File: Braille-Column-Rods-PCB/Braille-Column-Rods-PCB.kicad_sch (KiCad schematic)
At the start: 9 parts, among them J1 Conn_01x03, J5 Screw_Terminal_01x02, J6 Screw_Terminal_01x02, J7 Conn_01x02

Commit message: Polish prep for Rev 2 release, PCBA work
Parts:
- C9: now not fitted
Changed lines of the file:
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@@
 	(title_block
 		(title "Braille Cam Rod Prototype (Type 4)")
-		(date "2025-01-06")
-		(rev "Rev 1")
+		(date "2025-02-03")
+		(rev "Rev 2")
 	)
 	(junction
@@
 		(in_bom yes)
 		(on_board yes)
-		(dnp no)
+		(dnp yes)
 		(fields_autoplaced yes)
 		(property "Reference" "C9"

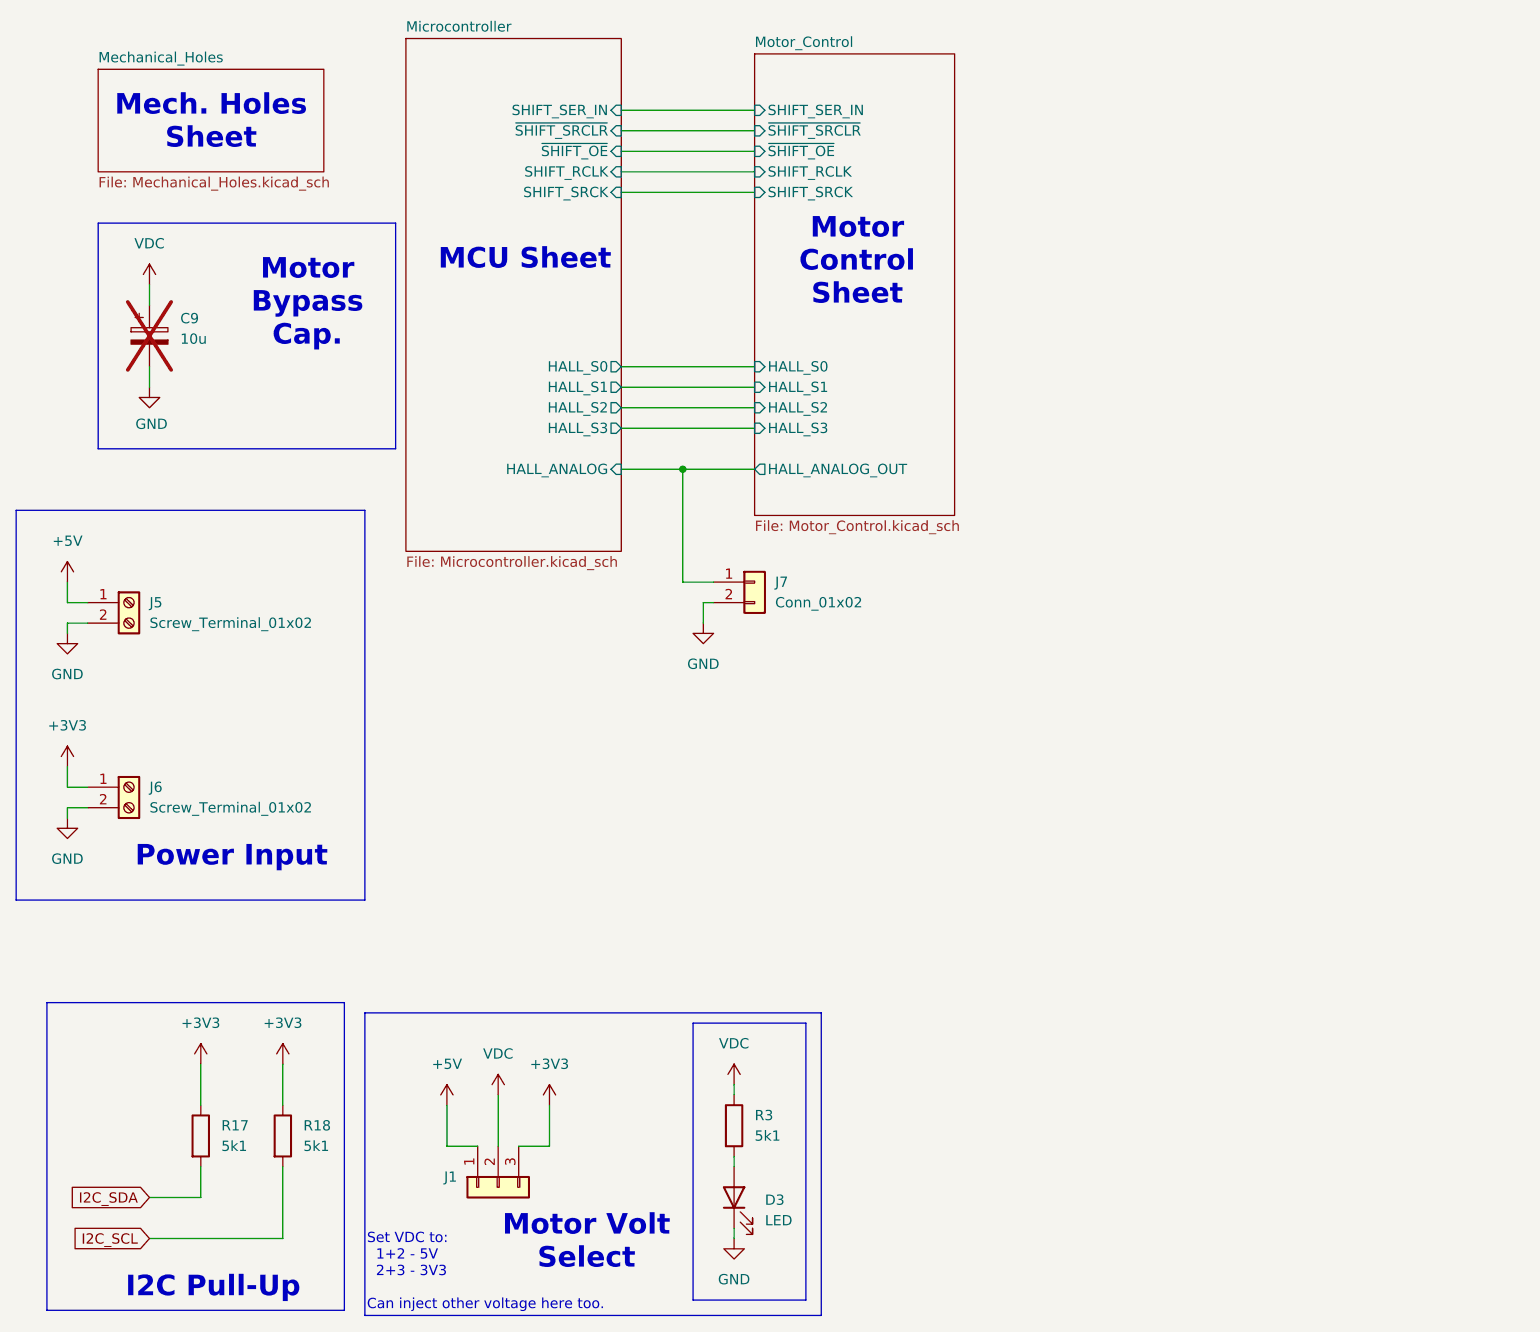
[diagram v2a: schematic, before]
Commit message: feat: add INA219 current sensor
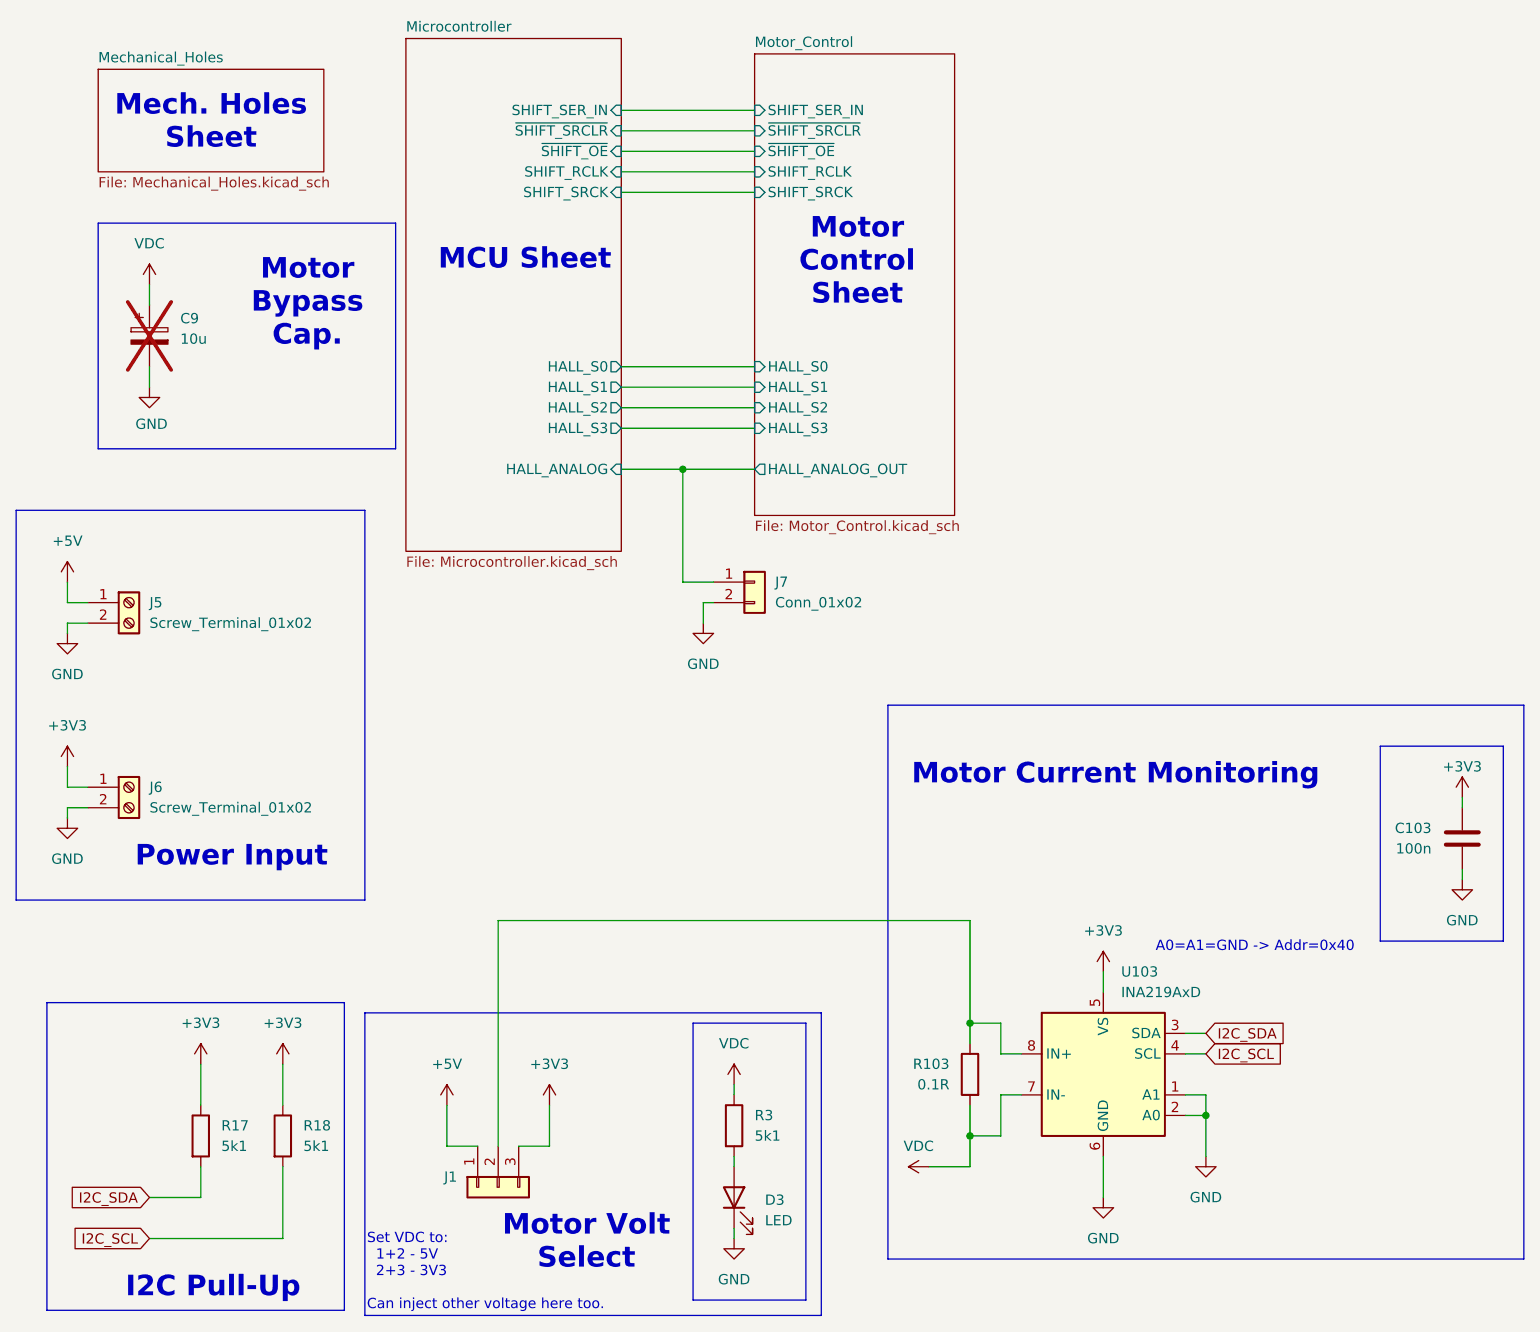
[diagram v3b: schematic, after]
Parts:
- added C103: 100n, Capacitor_SMD:C_0603_1608Metric_Pad1.08x0.95mm_HandSolder, symbol Device:C
- added R103: 0.1R, Resistor_SMD:R_1206_3216Metric_Pad1.30x1.75mm_HandSolder, symbol Device:R
- added U103: INA219AxD, Package_SO:SOIC-8_3.9x4.9mm_P1.27mm, symbol Sensor_Energy:INA219AxD
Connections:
- net +3V3: now also C103.1, U103.5 (VS)
- net GND: now also C103.2, U103.1 (A1), U103.2 (A0), U103.6 (GND)
- net I2C_SCL: now also U103.4 (SCL)
- net I2C_SDA: now also U103.3 (SDA)
- net VDC: now also R103.2, U103.7 (IN-); no longer J1.2 (Pin_2)
- new net: J1.2 (Pin_2), R103.1, U103.8 (IN+)
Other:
- note added: "A0=A1=GND -> Addr=0x40"
- note added: "Motor Current Monitoring"
